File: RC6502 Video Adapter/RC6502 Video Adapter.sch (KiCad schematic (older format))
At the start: 19 parts, among them J1 CONN_01X39, J2 CONN_02X20, J3 Video, J4 FTDI, J5 ICSP, U1 ATMEGA328P-PU, Y1 16 Mhz

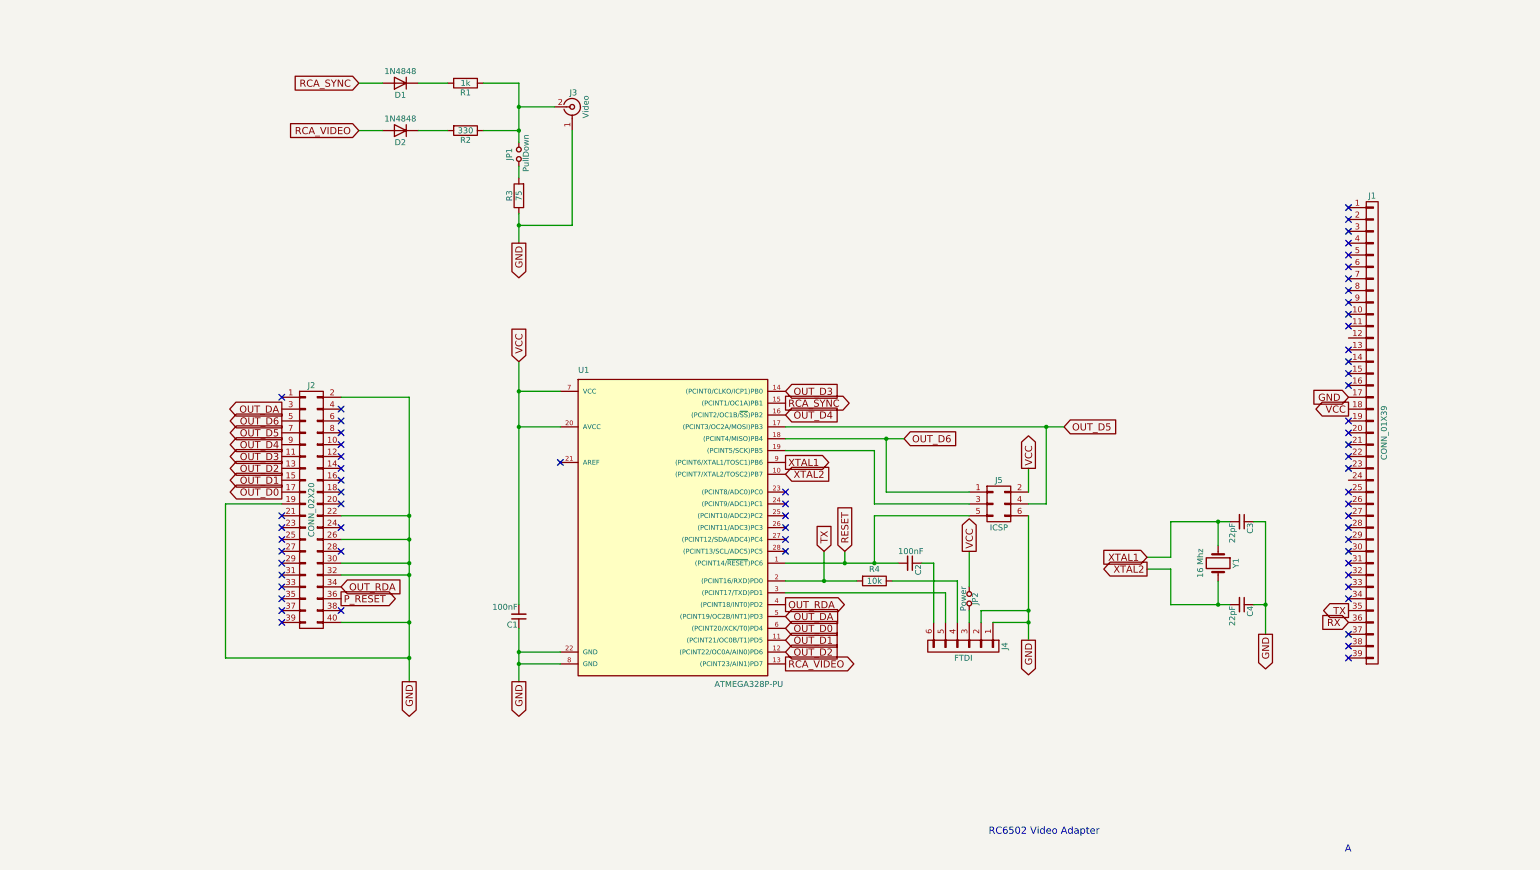
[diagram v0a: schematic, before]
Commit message: Video Adapter revision B
Adds IO expanders for possibly offloading the actual image output rendering to an analog module via a separate connector.
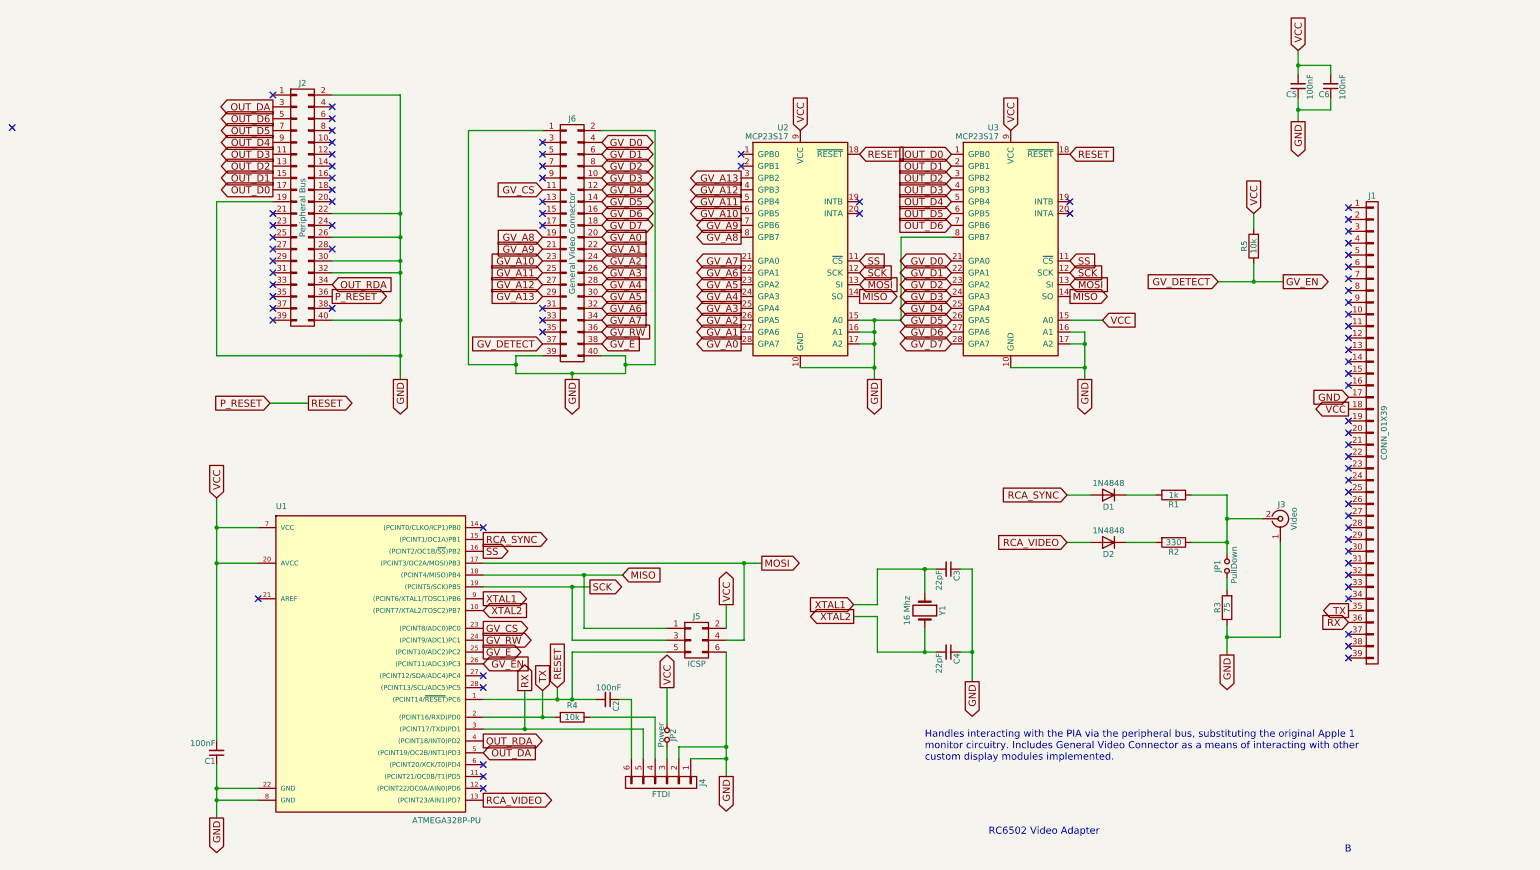
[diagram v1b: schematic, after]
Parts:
- added C5, C6: 100nF, Capacitors_THT:C_Disc_D4.7mm_W2.5mm_P5.00mm, symbol C_Small
- added J6: General Video Connector, Connectors:IDC_Header_Straight_40pins, symbol CONN_02X20
- added R5: 10k, Resistors_THT:R_Axial_DIN0207_L6.3mm_D2.5mm_P10.16mm_Horizontal, symbol R
- added U2, U3: MCP23S17, Housings_DIP:DIP-28_W7.62mm_Socket, symbol MCP23S17
- J2: value CONN_02X20 -> Peripheral Bus
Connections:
- net RESET is gone; now on net P_RESET: C2.2, J5.5 (P5), U1.1 ((PCINT14/~RESET~)PC6)
- net GND: now also C5.1, C6.1, J6.1 (P1), J6.2 (P2), J6.39 (P39), J6.40 (P40), U2.10 (GND), U2.15 (A0), U2.16 (A1), U2.17 (A2), U3.10 (GND), U3.16 (A1), U3.17 (A2), U3.8 (GPB7)
- net OUT_D0: now also U3.1 (GPB0); no longer U1.6 ((PCINT20/XCK/T0)PD4)
- net OUT_D1: now also U3.2 (GPB1); no longer U1.11 ((PCINT21/OC0B/T1)PD5)
- net OUT_D2: now also U3.3 (GPB2); no longer U1.12 ((PCINT22/OC0A/AIN0)PD6)
- net OUT_D3: now also U3.4 (GPB3); no longer U1.14 ((PCINT0/CLKO/ICP1)PB0)
- net OUT_D4: now also U3.5 (GPB4); no longer U1.16 ((PCINT2/OC1B/~SS~)PB2)
- net OUT_D5: now also U3.6 (GPB5); no longer J5.4 (P4), U1.17 ((PCINT3/OC2A/MOSI)PB3)
- net OUT_D6: now also U3.7 (GPB6); no longer J5.1 (P1), U1.18 ((PCINT4/MISO)PB4)
- net P_RESET: now also U2.18 (~RESET), U3.18 (~RESET)
- net RX: now also J4.5 (P5), U1.3 ((PCINT17/TXD)PD1)
- net VCC: now also C5.2, C6.2, R5.2, U2.9 (VCC), U3.15 (A0), U3.9 (VCC)
- net SCK: now reaches J5.3 (P3), U1.19 ((PCINT5/SCK)PB5)
- net SCK: now also U2.12 (SCK), U3.12 (SCK)
- net GV_CS: now reaches U1.23 ((PCINT8/ADC0)PC0)
- net GV_CS: now also J6.11 (P11)
- net GV_RW: now reaches U1.24 ((PCINT9/ADC1)PC1)
- net GV_RW: now also J6.36 (P36)
- net GV_E: now reaches U1.25 ((PCINT10/ADC2)PC2)
- net GV_E: now also J6.38 (P38)
- net GV_DETECT: now reaches U1.26 ((PCINT11/ADC3)PC3)
- net GV_DETECT: now also J6.37 (P37), R5.1
- new net GV_A0: J6.20 (P20), U2.28 (GPA7)
- new net GV_A1: J6.22 (P22), U2.27 (GPA6)
- new net GV_A10: J6.23 (P23), U2.6 (GPB5)
- new net GV_A11: J6.25 (P25), U2.5 (GPB4)
- new net GV_A12: J6.27 (P27), U2.4 (GPB3)
- new net GV_A13: J6.29 (P29), U2.3 (GPB2)
- new net GV_A2: J6.24 (P24), U2.26 (GPA5)
- new net GV_A3: J6.26 (P26), U2.25 (GPA4)
- new net GV_A4: J6.28 (P28), U2.24 (GPA3)
- new net GV_A5: J6.30 (P30), U2.23 (GPA2)
- new net GV_A6: J6.32 (P32), U2.22 (GPA1)
- new net GV_A7: J6.34 (P34), U2.21 (GPA0)
- new net GV_A8: J6.19 (P19), U2.8 (GPB7)
- new net GV_A9: J6.21 (P21), U2.7 (GPB6)
- new net GV_D0: J6.4 (P4), U3.21 (GPA0)
- new net GV_D1: J6.6 (P6), U3.22 (GPA1)
- new net GV_D2: J6.8 (P8), U3.23 (GPA2)
- new net GV_D3: J6.10 (P10), U3.24 (GPA3)
- new net GV_D4: J6.12 (P12), U3.25 (GPA4)
- new net GV_D5: J6.14 (P14), U3.26 (GPA5)
- new net GV_D6: J6.16 (P16), U3.27 (GPA6)
- new net GV_D7: J6.18 (P18), U3.28 (GPA7)
- new net MISO: J5.1 (P1), U1.18 ((PCINT4/MISO)PB4), U2.14 (SO), U3.14 (SO)
- new net MOSI: J5.4 (P4), U1.17 ((PCINT3/OC2A/MOSI)PB3), U2.13 (SI), U3.13 (SI)
- new net SS: U1.16 ((PCINT2/OC1B/~SS~)PB2), U2.11 (~CS), U3.11 (~CS)
- no-connect marks 63 -> 82
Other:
- note added: "B"
- note added: "Handles interacting with the PIA via the peripheral bus, substituting the original Apple 1\nmonitor circuitry. Includes General Video Connector as a means of interacting with other\ncustom display modules implemented."
- note removed: "A"
- moved on the sheet: C1, C2, C3, C4, D1, D2, J2, J3, J4, J5, JP1, JP2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

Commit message: Fixed video adapter rca connector footprint.
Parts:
- J3: footprint w_conn_av:rca_yellow -> rca:rca_yellow
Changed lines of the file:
@@
 F 0 "J3" H 10035 4945 50  0000 C CNN
 F 1 "Video" V 10140 4825 50  0000 C CNN
-F 2 "w_conn_av:rca_yellow" H 10025 4825 50  0001 C CNN
+F 2 "rca:rca_yellow" H 10025 4825 50  0001 C CNN
 F 3 "" H 10025 4825 50  0001 C CNN
 	1    10025 4825
